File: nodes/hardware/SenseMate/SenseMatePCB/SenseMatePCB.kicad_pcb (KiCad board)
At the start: 2 copper layers, 57.1 x 72.7 mm, 12 parts, among them M1 Motor_DC, Q1 2SC1815, Q2 2SC1815, SW5 SW_DPDT_x2

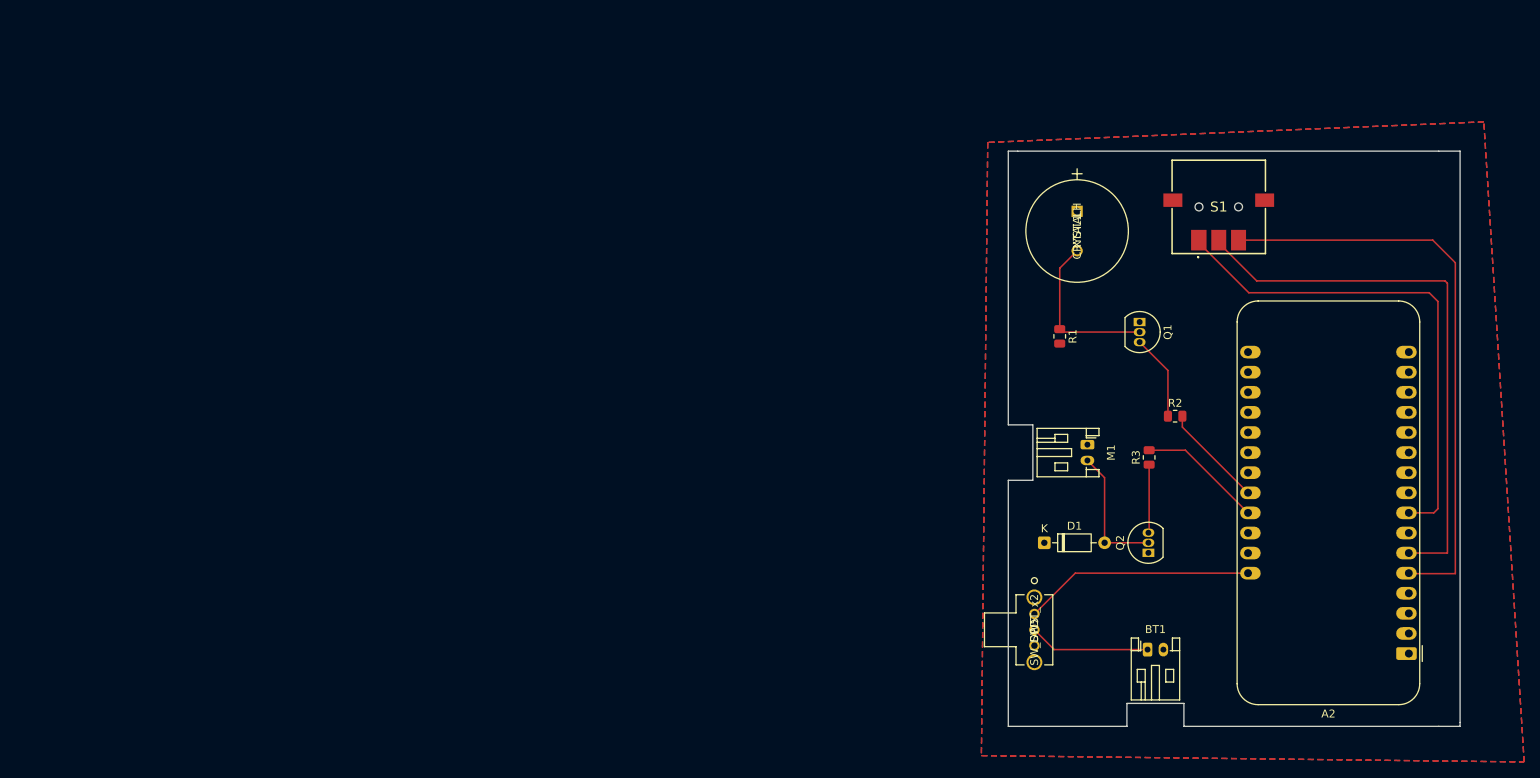
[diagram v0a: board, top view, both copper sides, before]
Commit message: moved switch button a littlebit mroe outside issue#4
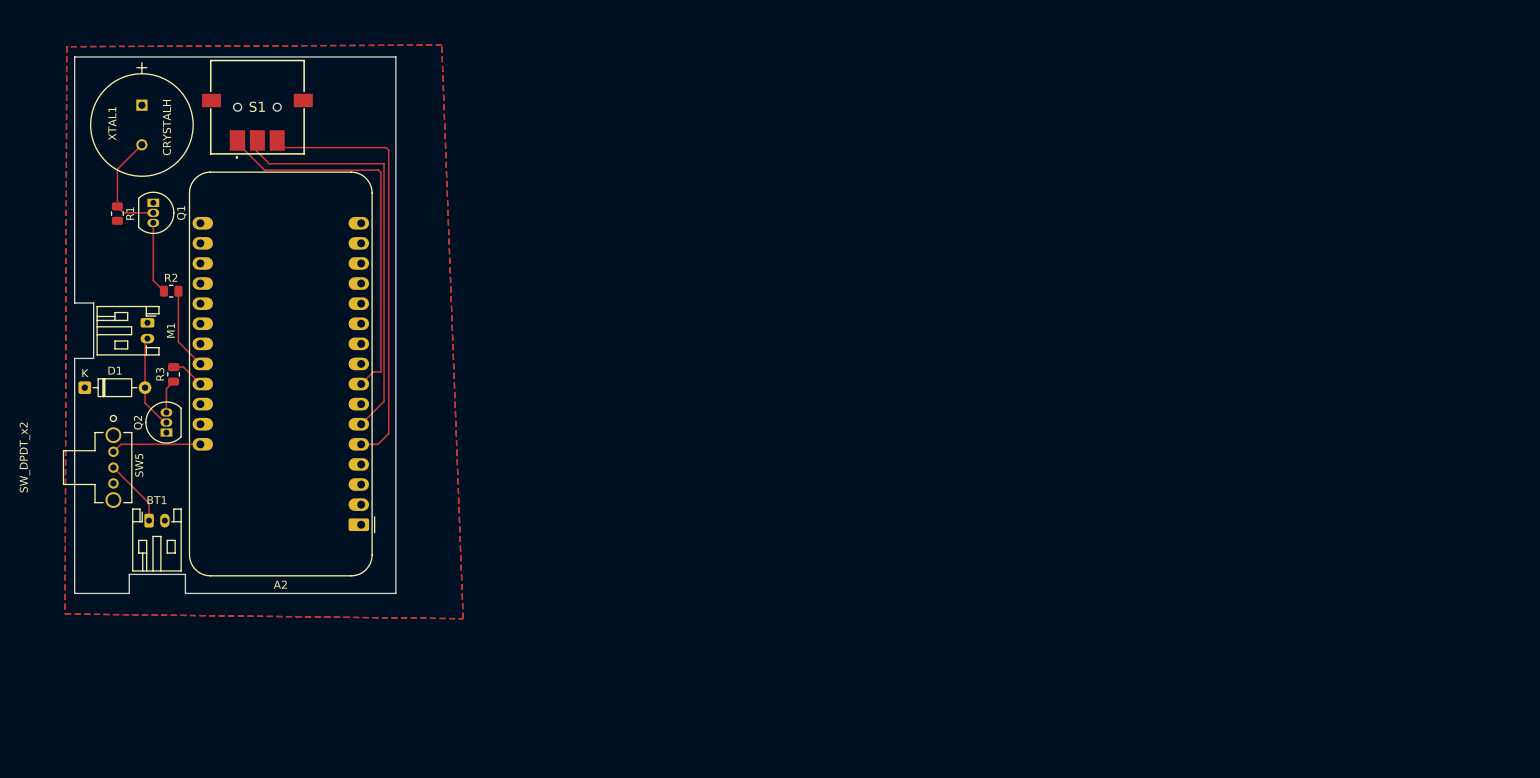
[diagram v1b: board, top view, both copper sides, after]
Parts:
- moved A2 133.4 mm to (115.7, 105.4)
- moved R2 127.9 mm to (91.7, 75.9)
- moved BT1 127.2 mm to (88.9, 104.9)
- moved Q1 125.6 mm to (89.4, 64.7)
- moved Q2 125.0 mm to (91.1, 93.8)
- moved R3 123.7 mm to (92.0, 86.4)
- moved D1 122.8 mm to (80.8, 88.1)
- moved S1 122.2 mm to (102.6, 52.6)
- moved R1 120.1 mm to (84.9, 66.1)
- moved M1 119.8 mm to (88.7, 79.9)
- moved XTAL1 119.0 mm to (88.0, 52.4)
- moved SW5 118.2 mm to (84.4, 96.2)
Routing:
- net Net-(A2-A0): track 73.8 -> 54.3 mm
- net Net-(A2-A1): track 70.3 -> 51.4 mm
- net Net-(A2-VBAT): track 29.1 -> 11.4 mm
- net Net-(A2-A3): track 63.7 -> 48.6 mm
- net Net-(A2-13): track 15.8 -> 4.28 mm
- net Net-(Q1-C): track 21.1 -> 13.9 mm
- net Net-(BT1-+): track 15.3 -> 8.56 mm
- net Net-(D1-A): track 17.0 -> 12.0 mm
- net Net-(Q2-B): track 8.64 -> 4.28 mm
- net Net-(A2-12): track 13.1 -> 10.3 mm
- net Net-(Q1-B): track 10.8 -> 9.19 mm
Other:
- board size 57.1 x 72.7 mm -> 40.6 x 67.8 mm

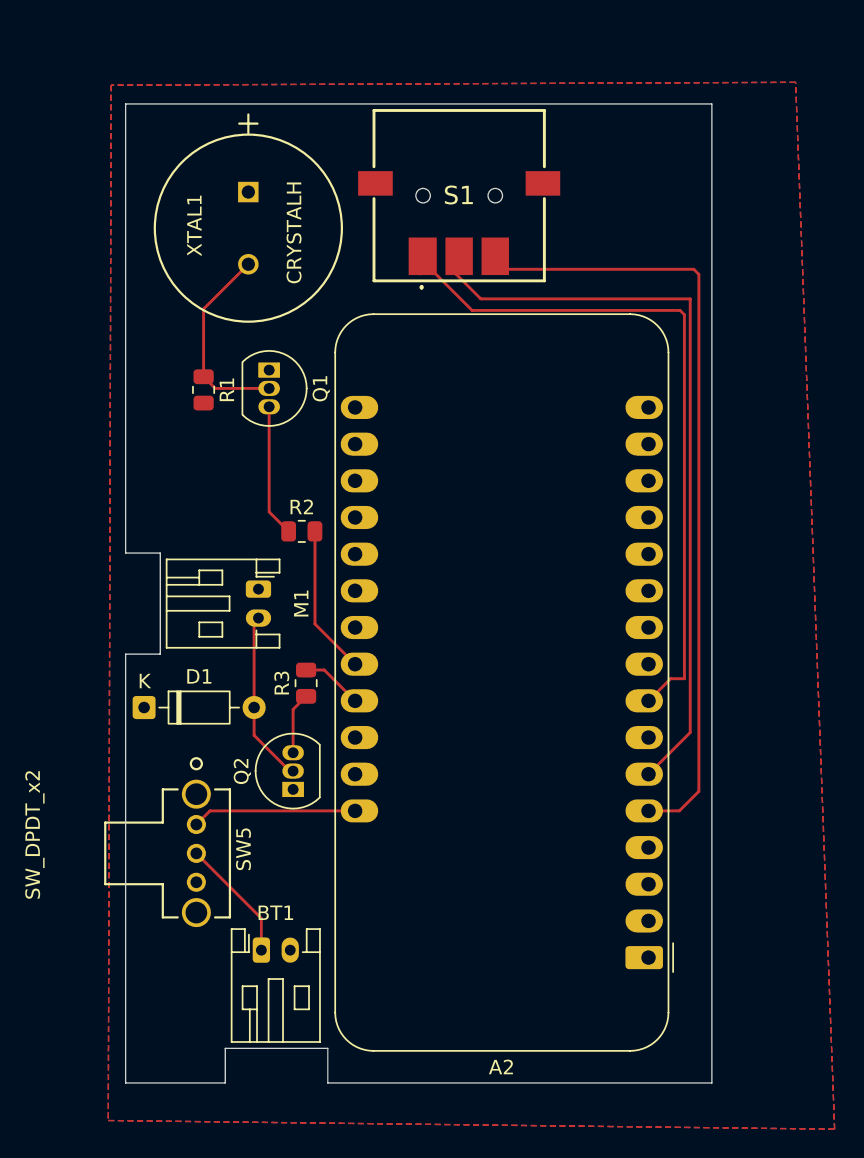
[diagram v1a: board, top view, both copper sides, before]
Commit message: run drc, resolved most error, still one because of 'no connection betwen gnd f and b' but already placed a via issue#5
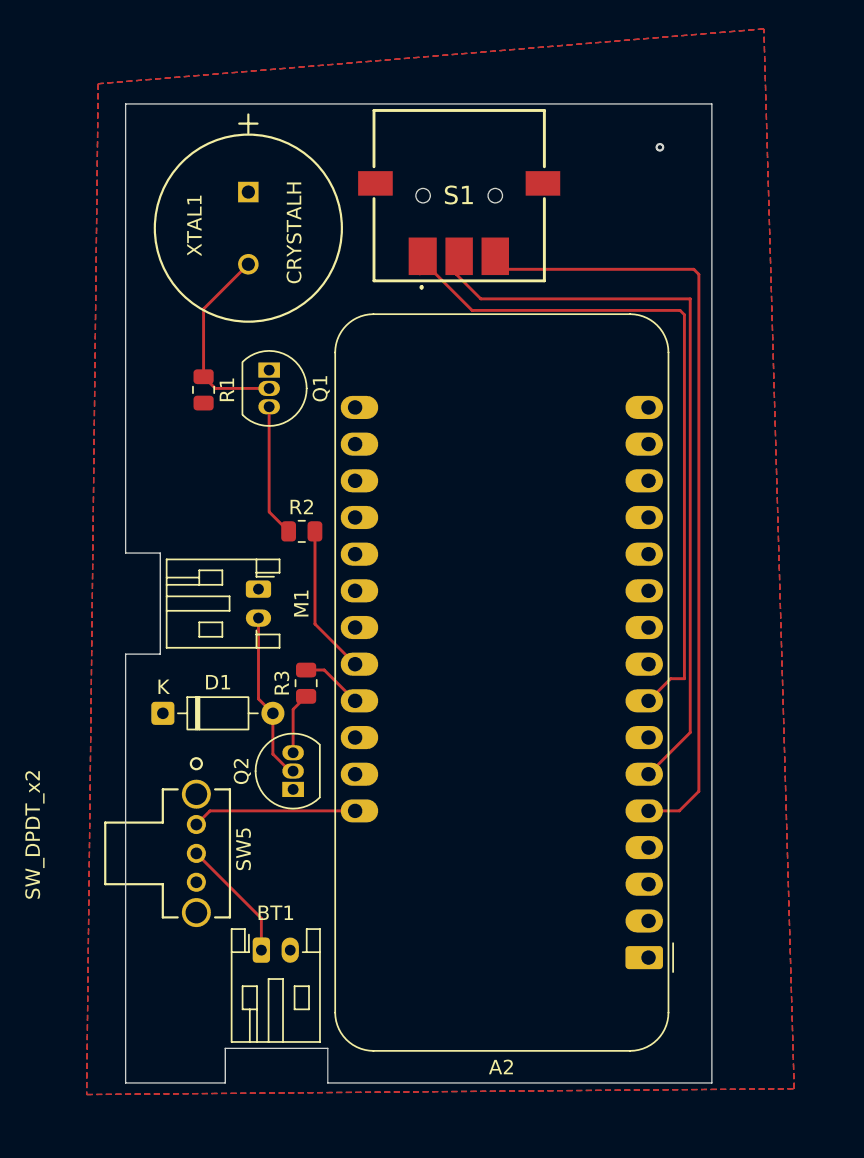
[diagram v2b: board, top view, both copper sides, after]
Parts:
- moved D1 1.36 mm to (82.1, 88.5)
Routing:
- net GND: vias 0 -> 1
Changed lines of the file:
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@@
 	(footprint "Diode_THT:D_DO-35_SOD27_P7.62mm_Horizontal"
 		(layer "F.Cu")
-		(at 80.78 88.1)
+		(at 82.08 88.5)
 		(descr "Diode, DO-35_SOD27 series, Axial, Horizontal, pin pitch=7.62mm, length*diameter=4*2mm^2, http://www.diodes.com/_files/packages/DO-35.pdf")
 		(tags "Diode DO-35_SOD27 series Axial Horizontal pin pitch 7.62mm  length 4mm diameter 2mm")
@@
 		(net 25)
 	)
+	(via
+		(at 116.5 49.3)
+		(size 0.6)
+		(drill 0.3)
+		(layers "F.Cu" "B.Cu")
+		(free yes)
+		(net 27)
+	)
 	(segment
 		(start 88.9 102.699999)
@@
 	(segment
 		(start 90.875 92.5)
-		(end 88.4 90.025)
+		(end 89.7 91.325)
 		(width 0.2)
 		(layer "F.Cu")
@@
 	)
 	(segment
-		(start 88.4 88.1)
-		(end 88.4 82.2)
+		(start 89.7 91.325)
+		(end 89.7 88.5)
+		(width 0.2)
+		(layer "F.Cu")
+		(net 30)
+	)
+	(segment
+		(start 88.7 87.5)
+		(end 89.7 88.5)
 		(width 0.2)
 		(layer "F.Cu")
@@
 	)
 	(segment
-		(start 88.4 90.025)
-		(end 88.4 88.1)
+		(start 88.7 81.9)
+		(end 88.7 87.5)
 		(width 0.2)
 		(layer "F.Cu")
@@
 		(layer "F.Cu")
 		(hatch edge 0.5)
-		(priority 1)
-		(connect_pads
+		(priority 2)
+		(connect_pads yes
 			(clearance 0.5)
 		)
@@
 		(polygon
 			(pts
-				(xy 78.5 45) (xy 78.3 116.7) (xy 128.6 117.3) (xy 125.9 44.8)
+				(xy 77.6 44.9) (xy 76.8 114.9) (xy 125.8 114.5) (xy 123.7 41.1)
 			)
 		)
@@
 		(polygon
 			(pts
-				(xy 78.5 45) (xy 78.3 116.7) (xy 128.6 117.3) (xy 125.9 44.8)
+				(xy 77.6 44.9) (xy 76.8 114.9) (xy 125.8 114.5) (xy 123.7 41.1)
 			)
 		)

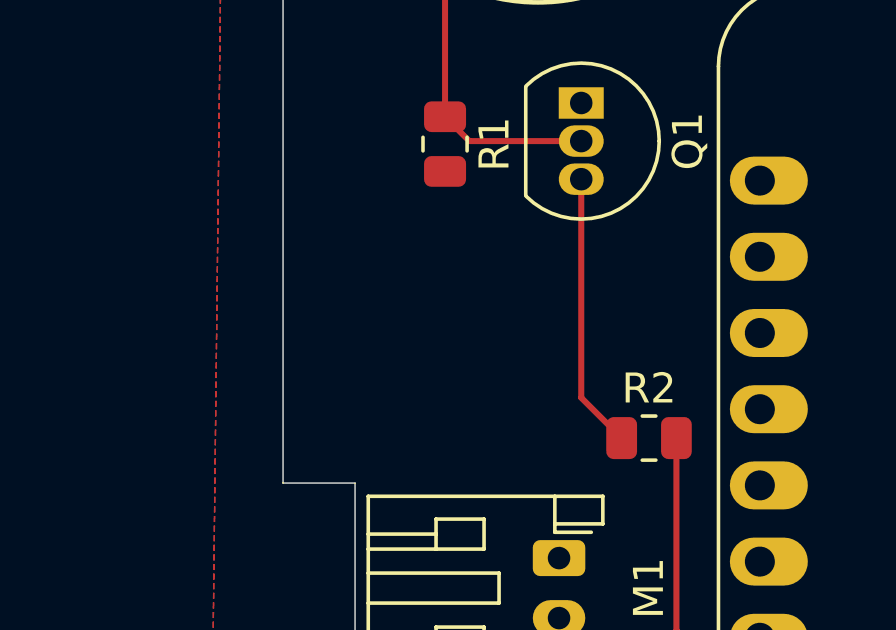
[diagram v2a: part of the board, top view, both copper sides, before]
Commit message: added logo and finished everything up, discussion for throughhols otherwise read for gerber files issue#6
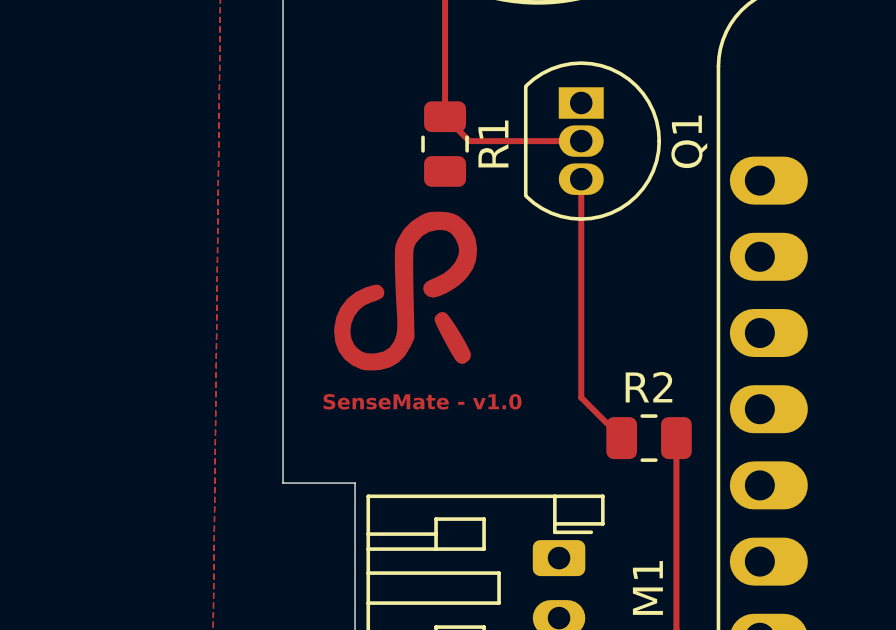
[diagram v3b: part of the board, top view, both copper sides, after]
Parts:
- added G***: LOGO, LOGO, F.Cu at (86.1, 71.0)
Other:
- board text added: "SenseMate - v1.0"
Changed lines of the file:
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@@
+		(embedded_fonts no)
+	)
+	(footprint "LOGO"
+		(layer "F.Cu")
+		(at 86.147416 70.995713)
+		(property "Reference" "G***"
+			(at -19.9 -2.2 0)
+			(layer "F.SilkS")
+			(hide yes)
+			(effects
+				(font
+					(size 1.5 1.5)
+					(thickness 0.3)
+				)
+			)
+		)
+		(property "Value" "LOGO"
+			(at 0.75 0 0)
+			(layer "F.SilkS")
+			(hide yes)
+			(effects
+				(font
+					(size 1.5 1.5)
+					(thickness 0.3)
+				)
+			)
+		)
+		(property "Datasheet" ""
+			(at 0 0 0)
+			(layer "F.Fab")
+			(hide yes)
+			(effects
+				(font
+					(size 1.27 1.27)
+					(thickness 0.15)
+				)
+			)
+		)
+		(property "Description" ""
+			(at 0 0 0)
+			(layer "F.Fab")
+			(hide yes)
+			(effects
+				(font
+					(size 1.27 1.27)
+					(thickness 0.15)
+				)
+			)
+		)
+		(attr board_only exclude_from_pos_files exclude_from_bom)
+		(fp_poly
+			(pts
+				(xy -1.227355 0.725396) (xy -1.162206 0.787085) (xy -1.06636 0.910782) (xy -0.949841 1.079926) (xy -0.822672 1.277955)
+				(xy -0.694878 1.488307) (xy -0.576484 1.694422) (xy -0.477512 1.879736) (xy -0.407988 2.02769) (xy -0.377935 2.121721)
+				(xy -0.377448 2.129587) (xy -0.419349 2.27064) (xy -0.494451 2.350273) (xy -0.601352 2.420878) (xy -0.692901 2.433404)
+				(xy -0.805844 2.398204) (xy -0.868949 2.338975) (xy -0.965357 2.199664) (xy -1.093947 1.982059)
+				(xy -1.253601 1.687947) (xy -1.267987 1.660583) (xy -1.399185 1.409043) (xy -1.493107 1.223284)
+				(xy -1.554449 1.090822) (xy -1.587907 0.99917) (xy -1.59818 0.935844) (xy -1.589963 0.888359) (xy -1.572284 0.851711)
+				(xy -1.468442 0.737492) (xy -1.339945 0.696722)
+			)
+			(stroke
+				(width 0)
+				(type solid)
+			)
+			(fill yes)
+			(layer "F.Cu")
+		)
+		(fp_poly
+			(pts
+				(xy -1.168791 -2.62628) (xy -0.951646 -2.573755) (xy -0.764085 -2.472862) (xy -0.578446 -2.312435)
+				(xy -0.546161 -2.27955) (xy -0.349332 -2.025089) (xy -0.230054 -1.743834) (xy -0.182403 -1.420419)
+				(xy -0.180982 -1.332169) (xy -0.214277 -1.018448) (xy -0.31517 -0.738439) (xy -0.491419 -0.475109)
+				(xy -0.647845 -0.306979) (xy -0.815371 -0.166881) (xy -1.017825 -0.031995) (xy -1.231926 0.085374)
+				(xy -1.434391 0.172924) (xy -1.601938 0.218353) (xy -1.648974 0.222027) (xy -1.808657 0.185221)
+				(xy -1.923637 0.086521) (xy -1.974999 -0.056492) (xy -1.97605 -0.08193) (xy -1.955082 -0.193083)
+				(xy -1.883491 -0.284486) (xy -1.748243 -0.367748) (xy -1.572876 -0.441023) (xy -1.30924 -0.572101)
+				(xy -1.085639 -0.746919) (xy -0.914593 -0.951072) (xy -0.80862 -1.170155) (xy -0.779049 -1.354371)
+				(xy -0.811983 -1.541586) (xy -0.898137 -1.73275) (xy -1.018536 -1.891937) (xy -1.096457 -1.955378)
+				(xy -1.21573 -2.012844) (xy -1.351486 -2.034585) (xy -1.495099 -2.031432) (xy -1.767734 -1.972762)
+				(xy -2.001646 -1.834173) (xy -2.196792 -1.61569) (xy -2.198078 -1.613795) (xy -2.244495 -1.53944)
+				(xy -2.275813 -1.465814) (xy -2.29498 -1.373745) (xy -2.304941 -1.244057) (xy -2.308644 -1.057578)
+				(xy -2.309092 -0.891484) (xy -2.307966 -0.667935) (xy -2.304835 -0.380635) (xy -2.300065 -0.054611)
+				(xy -2.294024 0.28511) (xy -2.287079 0.613498) (xy -2.286889 0.621677) (xy -2.264686 1.576398) (xy -2.389206 1.842831)
+				(xy -2.573474 2.153838) (xy -2.800904 2.387682) (xy -3.074557 2.546442) (xy -3.397491 2.632195)
+				(xy -3.574651 2.648193) (xy -3.75382 2.650176) (xy -3.911256 2.642456) (xy -4.014592 2.626695) (xy -4.018707 2.625418)
+				(xy -4.344759 2.477827) (xy -4.603069 2.273836) (xy -4.790966 2.017486) (xy -4.905777 1.712821)
+				(xy -4.944831 1.363882) (xy -4.940067 1.231469) (xy -4.8722 0.869678) (xy -4.727308 0.545293) (xy -4.512399 0.26699)
+				(xy -4.234483 0.043441) (xy -3.900567 -0.116678) (xy -3.832832 -0.138771) (xy -3.663788 -0.187322)
+				(xy -3.553584 -0.20862) (xy -3.477174 -0.204582) (xy -3.409517 -0.177127) (xy -3.40003 -0.171922)
+				(xy -3.306883 -0.078762) (xy -3.269323 0.045351) (xy -3.292404 0.167178) (xy -3.339367 0.22697)
+				(xy -3.424513 0.276023) (xy -3.561425 0.333049) (xy -3.677807 0.372311) (xy -3.913123 0.472223)
+				(xy -4.104641 0.624068) (xy -4.111213 0.630789) (xy -4.271034 0.846245) (xy -4.368358 1.087421)
+				(xy -4.402346 1.336319) (xy -4.37216 1.574939) (xy -4.276962 1.785282) (xy -4.17063 1.906553) (xy -4.026884 2.013382)
+				(xy -3.881653 2.070186) (xy -3.703421 2.085787) (xy -3.55743 2.078219) (xy -3.302638 2.019751) (xy -3.10236 1.891619)
+				(xy -2.957971 1.694774) (xy -2.903987 1.573286) (xy -2.867029 1.448256) (xy -2.84571 1.302975) (xy -2.838646 1.120738)
+				(xy -2.844449 0.884838) (xy -2.861734 0.578567) (xy -2.863338 0.554065) (xy -2.88096 0.246054) (xy -2.897013 -0.108099)
+				(xy -2.90978 -0.465727) (xy -2.917543 -0.78416) (xy -2.917785 -0.799302) (xy -2.921125 -1.063494)
+				(xy -2.920349 -1.25703) (xy -2.913425 -1.398039) (xy -2.898317 -1.504652) (xy -2.872993 -1.594998)
+				(xy -2.835419 -1.687209) (xy -2.812577 -1.737148) (xy -2.624092 -2.05294) (xy -2.37655 -2.307505)
+				(xy -2.09898 -2.491195) (xy -1.951252 -2.566889) (xy -1.830707 -2.611965) (xy -1.70355 -2.634175)
+				(xy -1.535989 -2.641268) (xy -1.443183 -2.641601)
+			)
+			(stroke
+				(width 0)
+				(type solid)
+			)
+			(fill yes)
+			(layer "F.Cu")
+		)
 		(embedded_fonts no)
 	)
@@
 		(layer "Edge.Cuts")
 	)
+	(gr_text "SenseMate - v1.0"
+		(at 80.8 75 0)
+		(layer "F.Cu")
+		(effects
+			(font
+				(size 0.5 0.5)
+				(thickness 0.125)
+				(bold yes)
+			)
+			(justify left bottom)
+		)
+	)
 	(segment
